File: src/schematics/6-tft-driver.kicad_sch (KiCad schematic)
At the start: 31 parts, among them Q601 NX6008NBKW, Q602 BC847BS, Q603 BC847BS, U601 TMUX1574RSV, U602 TMUX1574RSV, U603 TMUX1574RSV

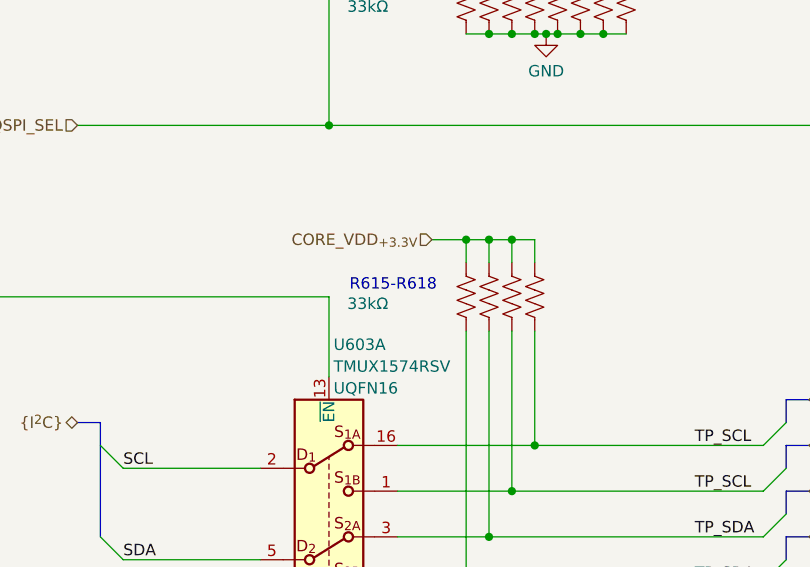
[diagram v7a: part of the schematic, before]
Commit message: Further elaboration of the circuitry surrounding the microcontroller.
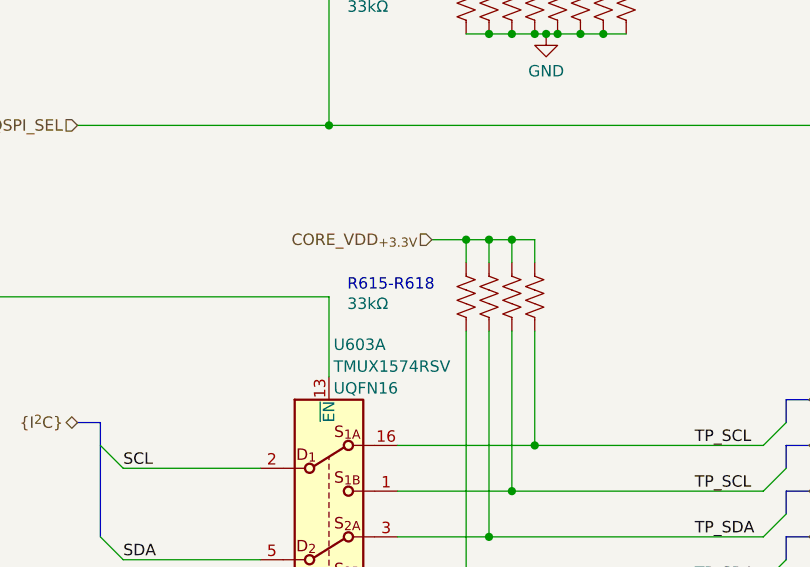
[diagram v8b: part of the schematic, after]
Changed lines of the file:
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@@
     (effects (font (size 2.54 2.54)) (justify left bottom))
   )
-  (text "R615-R618" (at 162.306 145.542 0)
+  (text "R615-R618" (at 162.052 145.542 0)
     (effects (font (size 1.27 1.27)) (justify left bottom))
   )
